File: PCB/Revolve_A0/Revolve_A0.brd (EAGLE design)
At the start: 100 x 100 mm, 383 parts, among them IC29 LAN8710A, IC30 MTFC2GMDEA, IC6 74AHC1G126DCK, IC7 74AHC1G126DCK, J2 4P-2.0, J3 4P-2.0, Q1 AON6758, Q10 DMC2038LVT, Q11 DMC2038LVT, Q13 DMC2038LVT, Q14 DMC2038LVT, Q2 AON6758, Q3 AON6758, Q8 AON6758, Q9 MMBT2907, U1 OSD3358-512M-BSM, U10 TPD4S012_DRY_6_P1_P, U11 SN74AHC595PW, U13 INA199A1DCKR, U19 CD4050BD, U2 TUSB2046BIRHBT, U3 TPS2061D, U4 TPD4S012_DRY_6_P1_P, U5 UA78L05ACD, U6 TPD4S012_DRY_6_P1_P, U7 TLVH431, U8 TPD4S012_DRY_6_P1_P, U9 TPD4S012_DRY_6_P1_P, X1 22-05-7038-03, X10 22-05-7038-03, X11 22-05-7038-03, X12 22-05-7048-04, X13 22-05-7038-03, X14 22-05-7048-04, X15 22-05-7048-04, X16 22-05-7048-04, X17 22-05-7048-04, X18 22-05-7048-04, X19 22-05-7038-03, X2 MSTBA4, X20 MSTBA4, X21 MSTBA2, X22 22-05-7038-03, X24 HDMI4, X25 22-05-7048-04, X26 MSTBA2, X29 22-05-7038-03, X3 MSTBA2, X4 22-05-7028-02, X5 22-05-7028-02, X6 22-05-7028-02, X7 22-05-7038-03, X8 22-05-7038-03, X9 22-05-7028-02, Y1 25MHz, Y2 25MHz, Y4 6 MHz

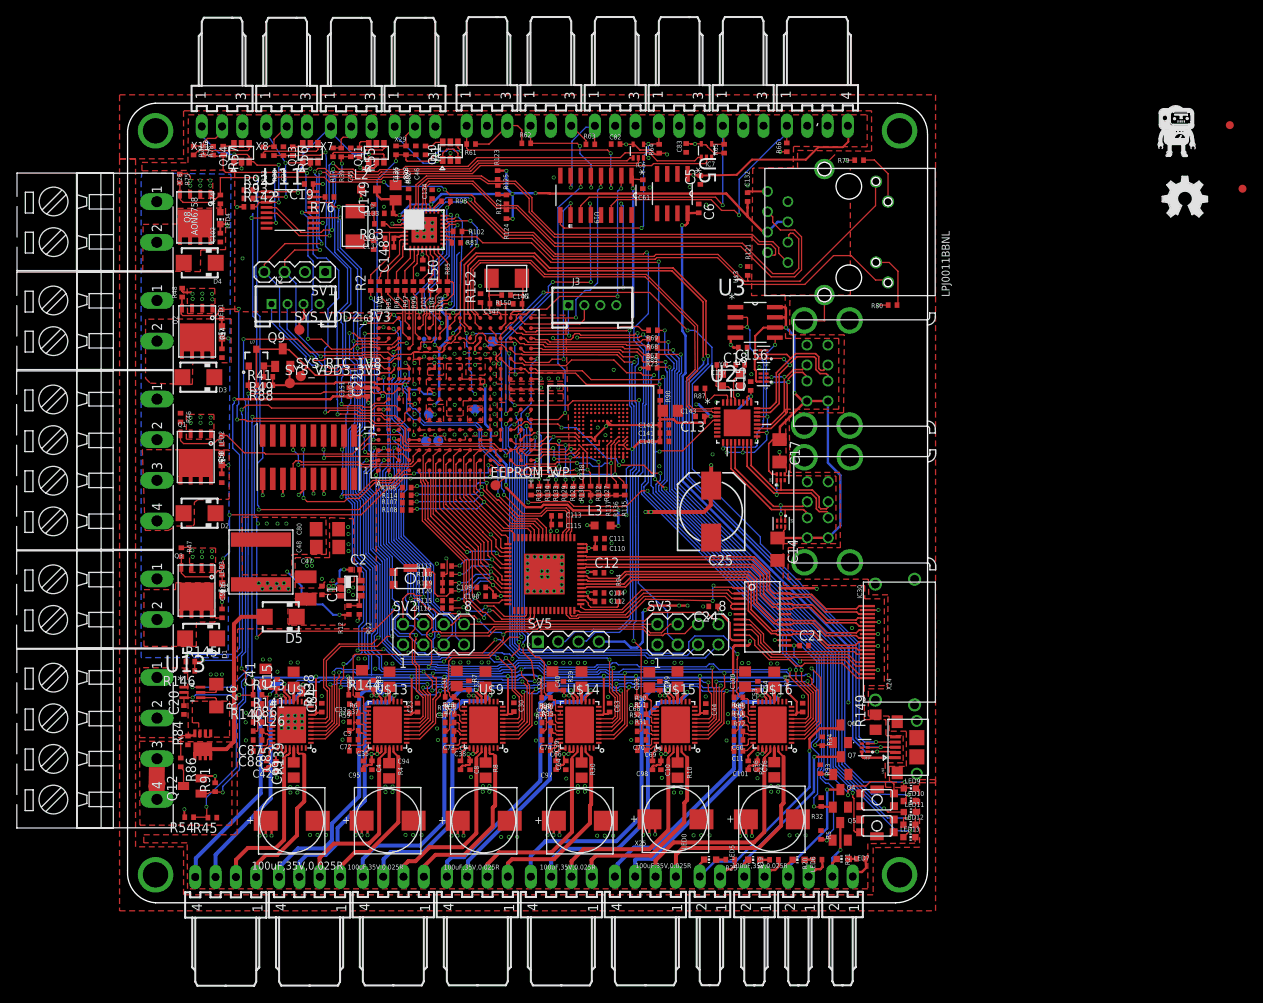
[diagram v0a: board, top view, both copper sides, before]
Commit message: DRC done, time to start documentation
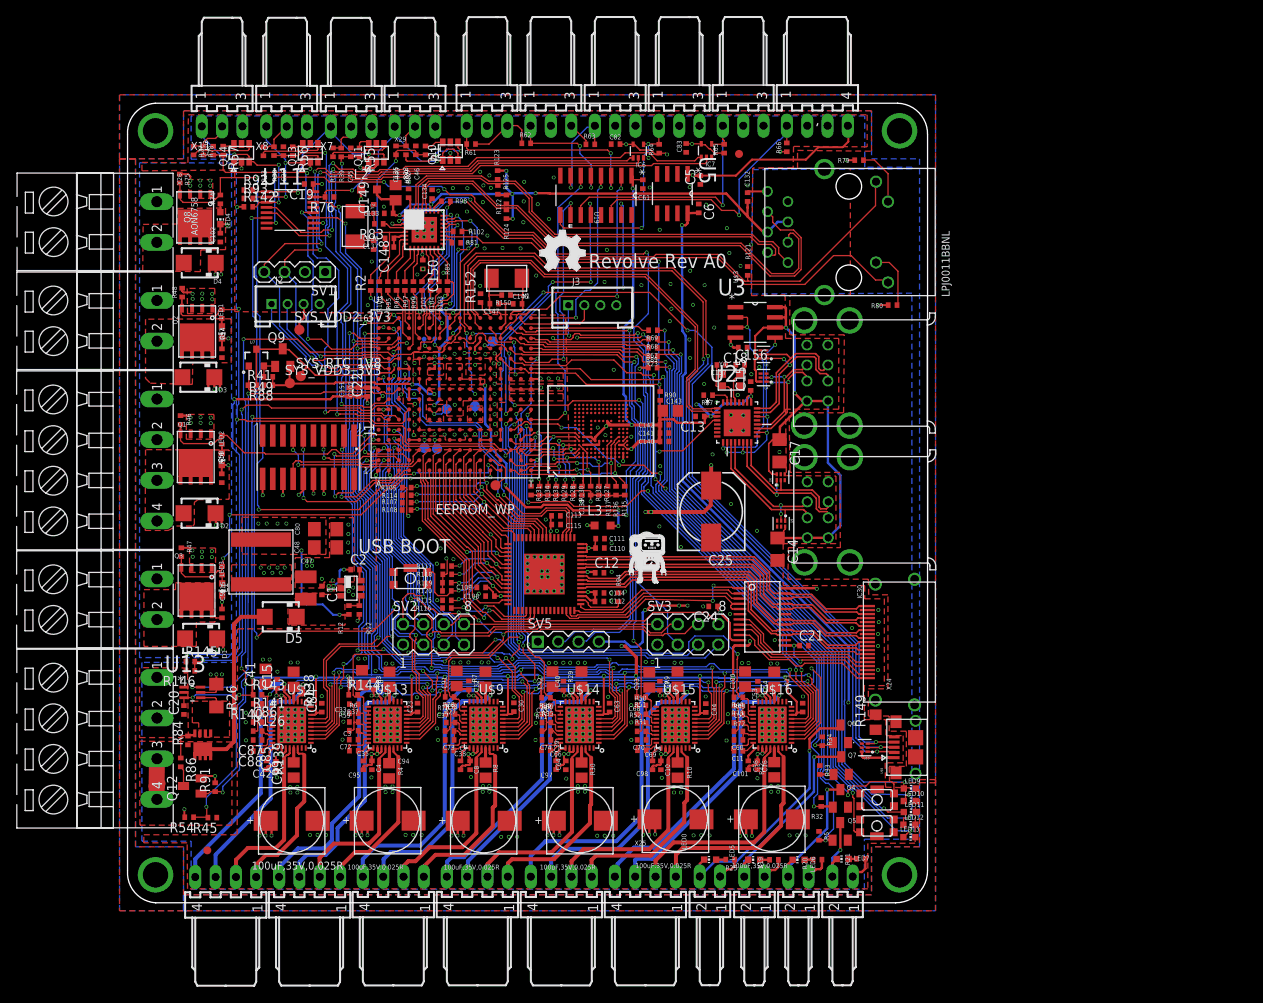
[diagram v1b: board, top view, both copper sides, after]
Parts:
- moved JP2 153.6 mm to (9.97, 6.56)
- moved U$1 85.0 mm to (64.5, 43.2)
- moved LOGO1 78.1 mm to (51.5, 79.0)
- moved JP1 61.5 mm to (76.4, 93.6)
- moved SYS_VDD1_3V3 2.29 mm to (39.9, 61.7)
- moved R87 1.27 mm to (72.6, 63.5)
- moved VDD_CODE 1.01 mm to (38.7, 56.7)
- moved VDDS_DDR 0.86 mm to (37.1, 56.9)
- moved SYS_5V 0.40 mm to (43.4, 62.1)
- moved R46 0.30 mm to (6.62, 60.4)
- moved R5 0.27 mm to (86.4, 8.38)
- moved C48 0.25 mm to (24.8, 44.4)
- moved C80 0.22 mm to (24.8, 46.7)
- moved U$8 0.15 mm to (98.5, 19.4)
- moved C37 0.13 mm to (40.4, 22.5)
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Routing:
- net SYS_VDD1_3V3: track 256.2 -> 285.6 mm, vias 29 -> 32
- net +24V: track 187.7 -> 206.2 mm, vias 48 -> 59
- net TRSTN: track 6.53 -> 20.0 mm, vias 0 -> 2
- net EN_TK_E: track 14.2 -> 27.2 mm, vias 1 -> 2
- net CGND: track 8.14 -> 0.00 mm
- net GND: track 52.4 -> 44.4 mm, vias 261 -> 458
- net EN_TK_HBP: track 15.9 -> 19.5 mm
- net TERM_E: track 34.2 -> 36.7 mm
- net +5V: track 20.7 -> 22.7 mm
- net N$40: track 0.00 -> 1.86 mm, vias 0 -> 1
- net N$192: track 4.44 -> 2.59 mm
- net MII1_TXCLK: track 12.3 -> 14.1 mm, vias 2 -> 4
- net N$34: track 0.00 -> 1.63 mm, vias 0 -> 1
- net HEATER_HBP: track 45.9 -> 47.5 mm
- net N$130: track 0.00 -> 1.11 mm
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- added copper zone on layer 16, net CGND
- added copper zone on layer 16, net GND
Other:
- board text added: "Revolve Rev A0"
- board text added: "USB BOOT"

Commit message: REady for board review
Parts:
- added C27: 0.1uF, rcl:C0402
- PMIC_NRESET, SYS_5V, SYS_VDD1_3V3, VDDS_DDR, VDD_CODE: value TPB1,27 -> TPTP06R; device testpad:B1,27 -> testpad:TP06R
- moved U$1 38.4 mm to (59.7, 81.3)
- moved JP1 17.3 mm to (93.2, 98.1)
- moved JP2 6.76 mm to (3.37, 8.01)
- moved R25 4.00 mm to (71.3, 5.41)
- moved R19 3.85 mm to (77.0, 5.43)
- moved R20 3.75 mm to (82.5, 5.50)
- moved R21 3.60 mm to (88.1, 5.39)
- moved LED0 3.24 mm to (70.7, 2.92), turned to 180 degrees
- moved LED5 2.92 mm to (76.4, 3.19), turned to 180 degrees
- moved LED7 2.80 mm to (87.5, 3.40), turned to 180 degrees
- moved LED6 2.80 mm to (82.0, 3.33), turned to 180 degrees
- moved SYS_VDD1_3V3 2.79 mm to (40.9, 64.3)
- moved VDD_MPU 2.15 mm to (37.1, 72.6)
- moved VDD_CODE 1.66 mm to (38.4, 55.1)
- moved C82 1.29 mm to (62.2, 94.3), turned to 270 degrees
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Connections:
- net GND: now also C27.2
- net SYS_VDD1_3V3: now also C27.1
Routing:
- net +24V: track 206.2 -> 213.7 mm
- net SYS_5V: track 51.5 -> 46.6 mm
- net SYS_VDD1_3V3: track 285.6 -> 289.4 mm
- net TXP: track 62.3 -> 65.4 mm
- net VDD_MPU: track 1.56 -> 3.71 mm
- net RXN: track 54.9 -> 56.5 mm
- net N$40: track 1.86 -> 3.37 mm
- net N$115: track 17.2 -> 16.0 mm
- net FAULT_E: track 41.7 -> 42.9 mm
- net N$114: track 9.59 -> 8.55 mm
- net VDDS_PLL: track 1.51 -> 2.41 mm
- net N$116: track 24.3 -> 23.5 mm
- net FAULT_Y: track 62.4 -> 63.2 mm
- net N$34: track 1.63 -> 2.33 mm
- net SERVO_1_EN: track 66.7 -> 67.3 mm
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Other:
- board text added: "A"
- board text added: "BOOT"
- board text added: "ENDSTOPS (S/-/+)"
- board text added: "FANS (- / +)"
- board text added: "HEATERS"
- board text added: "INPUT (++/--) 24V MAX"
- board text added: "QUAD ENCODER"
- board text added: "RESET"
- board text added: "Rev A0"
- board text added: "Revolve"
- board text added: "STEPPER B"
- board text added: "STEPPER C"
- board text added: "STEPPERS (AABB)"
- board text added: "THERMISTORS (+/S/-)"
- board text removed: "20A"
- board text removed: "Fuse"
- board text removed: "Revolve Rev A0"

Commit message: Added readme
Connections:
- net CLKOUT2_48MHZ renamed UNUSED_1
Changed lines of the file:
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@@
 <layer number="24" name="bOrigins" color="15" fill="1" visible="no" active="yes"/>
 <layer number="25" name="tNames" color="7" fill="1" visible="yes" active="yes"/>
-<layer number="26" name="bNames" color="7" fill="1" visible="no" active="yes"/>
+<layer number="26" name="bNames" color="7" fill="1" visible="yes" active="yes"/>
 <layer number="27" name="tValues" color="7" fill="1" visible="no" active="yes"/>
 <layer number="28" name="bValues" color="7" fill="1" visible="no" active="yes"/>
@@
 <attribute name="SPN" value="568-12059-ND" x="52.1" y="41.09" size="1.778" layer="27" display="off"/>
 <attribute name="MPN" value="TDA19988BHN/C1,518" x="52.1" y="41.09" size="1.778" layer="27" display="off"/>
-<attribute name="NAME" x="48.95" y="46.84" size="1.27" layer="26"/>
 <attribute name="VALUE" x="46.85" y="34.09" size="1.27" layer="27"/>
 </element>
@@
 <wire x1="87" y1="39.25" x2="86.15" y2="39.25" width="0.3" layer="1"/>
 </signal>
-<signal name="CLKOUT2_48MHZ">
+<signal name="UNUSED_1">
 <contactref element="U1" pad="B4"/>
 </signal>

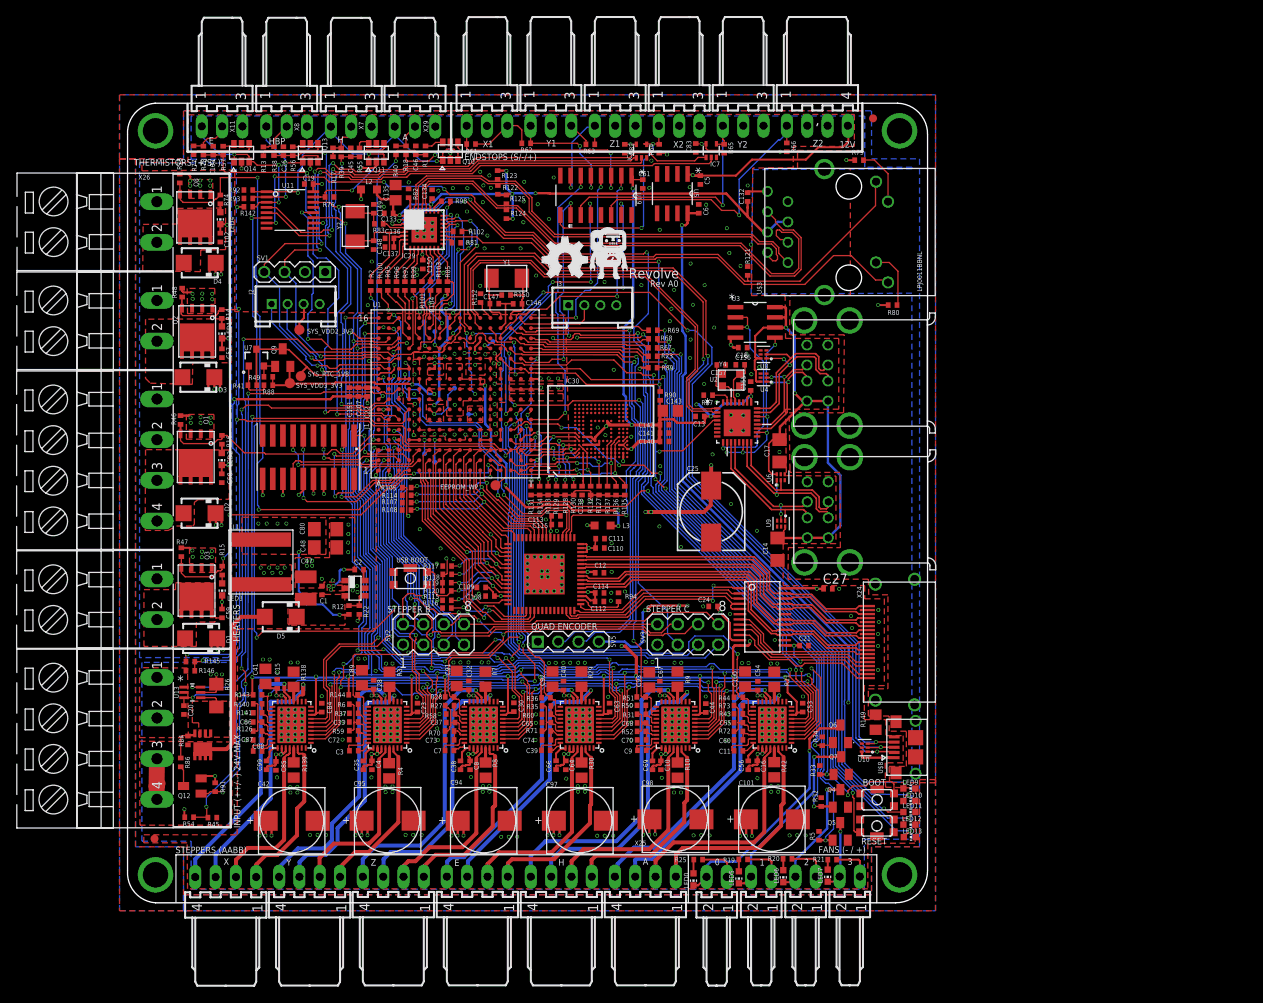
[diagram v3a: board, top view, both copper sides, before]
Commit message: Added calculations on PMOS to readme
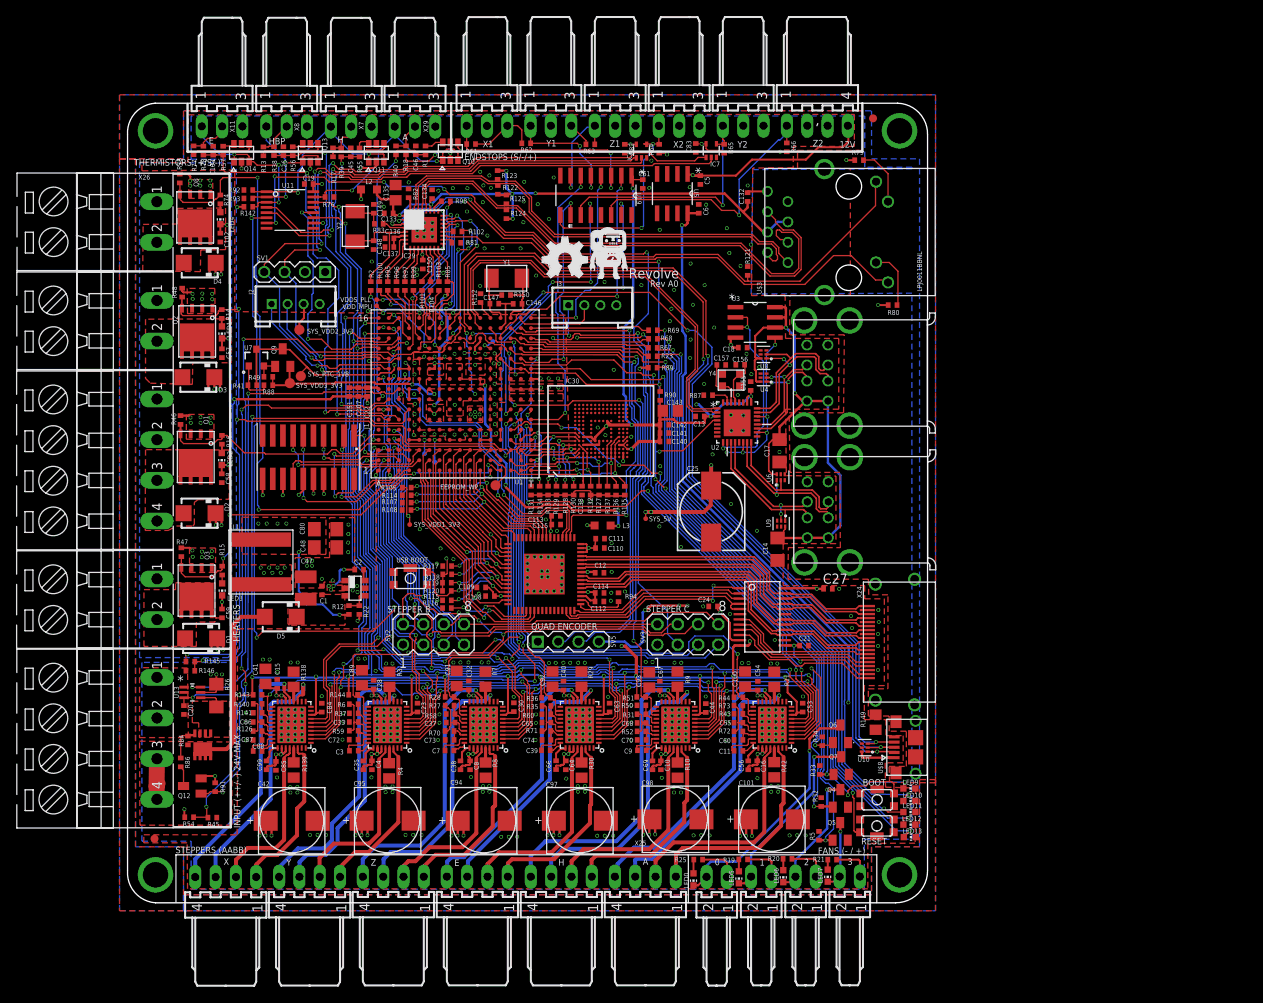
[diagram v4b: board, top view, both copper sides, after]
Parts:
- moved SYS_5V 25.7 mm to (64.8, 48.0), flipped to the top
- moved SYS_VDD1_3V3 17.9 mm to (35.3, 47.3), flipped to the top
- moved VDDS_PLL 8.30 mm to (31.1, 75.4), flipped to the top
- moved VDD_MPU 6.27 mm to (31.1, 74.6), flipped to the top
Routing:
- net VDDS_PLL: track 2.41 -> 12.1 mm, vias 1 -> 2
- net VDD_MPU: track 3.71 -> 10.1 mm, vias 1 -> 2
- net SYS_VDD1_3V3: track 289.4 -> 285.8 mm
- net SYS_5V: vias 12 -> 15

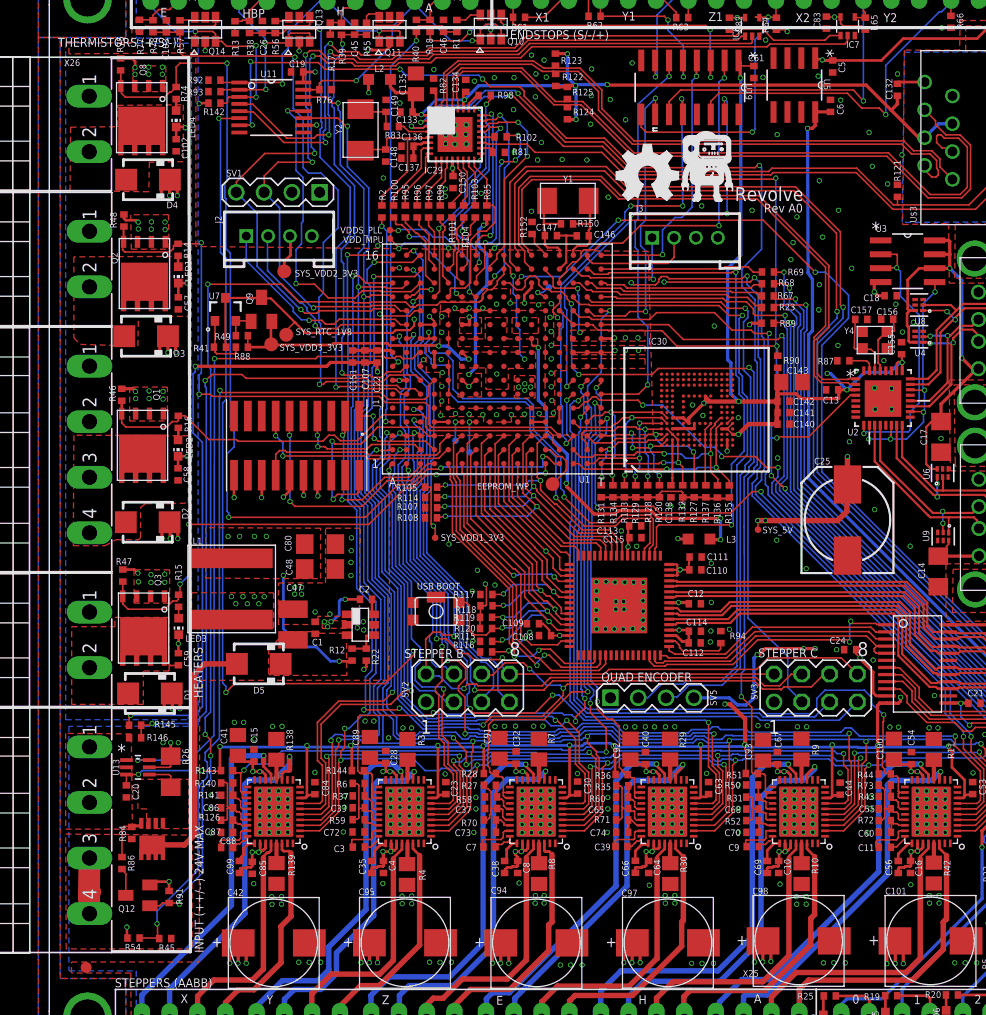
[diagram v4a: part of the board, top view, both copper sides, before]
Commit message: Ordered PCB and stencil + parts from OSH park/Digi key
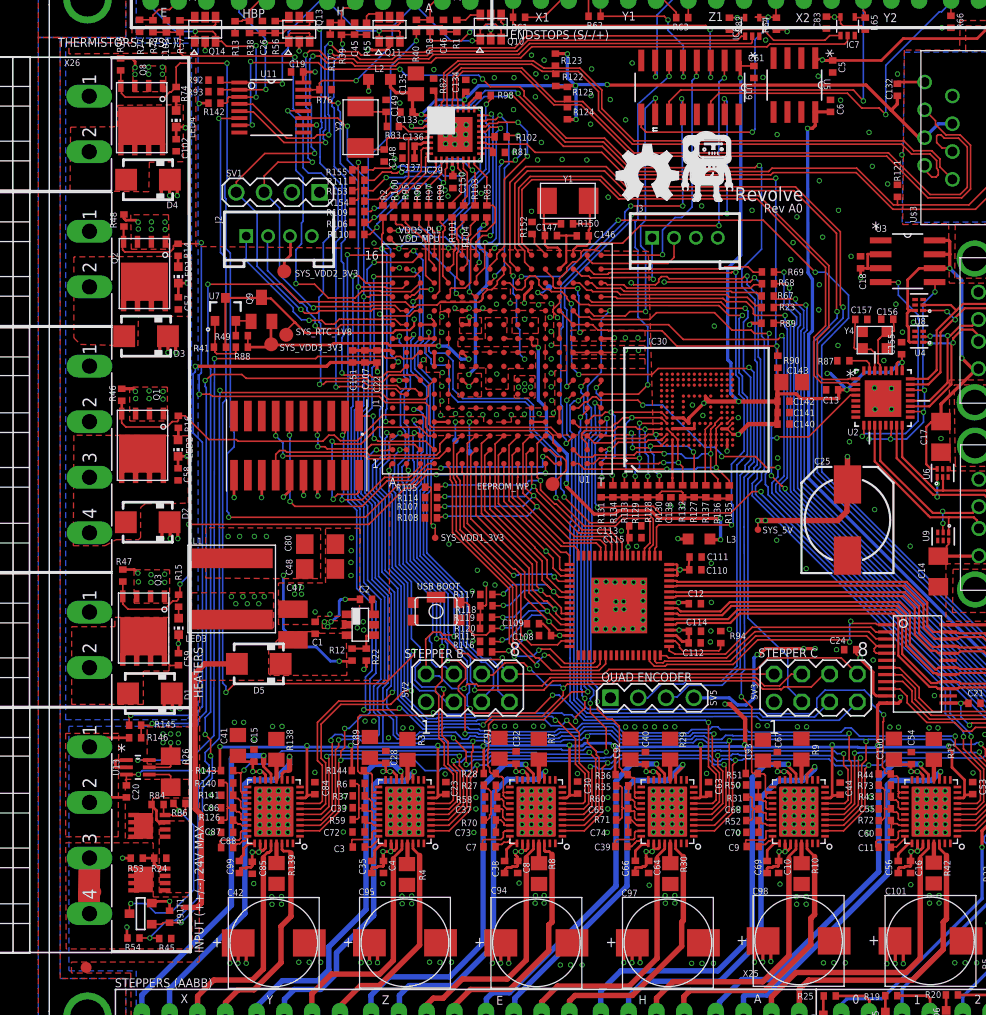
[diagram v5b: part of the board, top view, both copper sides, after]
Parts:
- removed Q12: (no value), semicon-smd-ipc:SOT23
- added R106, R109, R110, R111, R153, R154, R155, R53: 1K,1%, rcl:R0402
- added R24: 4.7K,1%, rcl:R0402
- added T1: (no value), zetex:SOT-23
- added U$11: SISS27DN, Revolve:POWERPAK-1212-8S
- R86: value 100K,1% -> 40.2K,1%
- moved R86 7.57 mm to (11.9, 23.0), turned to 180 degrees
- moved C18 4.11 mm to (74.2, 72.5), turned to 270 degrees
- moved U$17 3.71 mm to (9.15, 16.1), turned to 180 degrees
- moved R84 3.50 mm to (9.90, 22.9), turned to 0 degrees
- moved R91 1.80 mm to (11.0, 12.7)
- moved Y2 0.25 mm to (28.4, 84.8)
- moved C148 0.15 mm to (30.6, 82.2)
- moved C136 0.10 mm to (32.8, 83.1)
- moved C137 0.10 mm to (32.8, 82.0)
- moved R2 0.10 mm to (30.5, 77.1)
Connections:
- removed net N$212: IC29.8, R95.1
- removed net N$225: IC29.9, R96.1
- removed net N$226: IC29.10, R97.1
- removed net N$227: IC29.11, R99.1
- removed net N$229: IC29.7, R100.1
- removed net N$230: IC29.13, R101.1
- removed net N$239: IC29.15, R103.1
- new net MODE2: IC29.15, R103.1, R155.2
- new net N$17: R24.2, R53.1, U$17.G
- new net REFCLK0: IC29.7, R100.1, R106.2
- new net RXD0: IC29.11, R153.2, R99.1
- new net RXD1: IC29.10, R154.2, R97.1
- new net RXD2: IC29.9, R109.2, R96.1
- new net RXD3: IC29.8, R110.2, R95.1
- new net RXER: IC29.13, R101.1, R111.2
- new net VMID: R24.1, R84.1, U$11.S1, U$11.S2, U$11.S3, U$17.S1, U$17.S2, U$17.S3
- net ENABLE_STUFF: now also T1.3; no longer Q12.1
- net GND: now also R106.1, R109.1, R110.1, R111.1, R53.2, T1.2; no longer Q12.2
- net N$26: now also U$11.G; no longer U$17.G
- net N$8: now also T1.1; no longer Q12.3
- net P-SHUNT: now also U$11.D1, U$11.D2, U$11.D3, U$11.D4, U$11.D5; no longer U$17.S1, U$17.S2, U$17.S3
- net SYS_5V: now also U3.2, U3.3; no longer U3.4
- net SYS_VDD1_3V3: now also R153.1, R154.1, R155.1
- net USB_PWR: now also U3.4; no longer U3.2, U3.3
- net VIN: no longer R84.1
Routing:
- net MODE2: track 0.00 -> 15.2 mm, vias 0 -> 2
- net RXER: track 0.00 -> 14.1 mm, vias 0 -> 2
- net N$8: track 2.52 -> 16.6 mm, vias 0 -> 2
- net RXD0: track 0.00 -> 12.4 mm, vias 0 -> 2
- net RXD1: track 0.00 -> 11.3 mm, vias 0 -> 2
- net RXD3: track 0.00 -> 11.0 mm, vias 0 -> 2
- net REFCLK0: track 0.00 -> 10.9 mm, vias 0 -> 2
- net RXD2: track 0.00 -> 10.9 mm, vias 0 -> 2
- net GND: track 44.4 -> 55.3 mm, vias 460 -> 461
- net N$229: track 6.91 -> 0.00 mm
- net N$212: track 5.65 -> 0.00 mm
- net SYS_VDD1_3V3: track 285.8 -> 290.7 mm, vias 32 -> 33
- net N$225: track 4.85 -> 0.00 mm
- net N$230: track 4.64 -> 0.00 mm
- net N$226: track 4.62 -> 0.00 mm
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- added copper zone on layer 1, net +24V
- added copper zone on layer 1, net VMID
